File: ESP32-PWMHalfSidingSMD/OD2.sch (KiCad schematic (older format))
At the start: 5 parts, among them IC2 MCT6H, T6 In Track1 Out

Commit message: Update part numbers for ESP32-PWMHalfSidingSMD and created prelim BOM files.
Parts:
- R5: Mouser Part Number 603-CFR-25JR-5210R -> 71-CRCW060310R0FKEAC
- R6: Mouser Part Number 603-CFR25SJT-52-10K -> 71-CRCW060310K0JNEBC
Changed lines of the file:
@@
 F 2 "~" V 2430 1500 30  0000 C CNN
 F 3 "~" H 2500 1500 30  0000 C CNN
-F 4 "603-CFR-25JR-5210R" H 2500 1500 60  0001 C CNN "Mouser Part Number"
+F 4 "71-CRCW060310R0FKEAC" H 2500 1500 60  0001 C CNN "Mouser Part Number"
 	1    2500 1500
 	0    -1   -1   0
@@
 F 2 "~" V 4230 1100 30  0000 C CNN
 F 3 "~" H 4300 1100 30  0000 C CNN
-F 4 "603-CFR25SJT-52-10K" H 4300 1100 60  0001 C CNN "Mouser Part Number"
+F 4 "71-CRCW060310K0JNEBC" H 4300 1100 60  0001 C CNN "Mouser Part Number"
 	1    4300 1100
 	1    0    0    -1

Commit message: Updated ESP32-PWMHalfSidingSMD board.
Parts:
- added D7: LED, LEDs:LED_0603, symbol LED
- added Q2: MMBT3904, TO_SOT_Packages_SMD:SOT-23, symbol MMBT3904
- D5: footprint ~ -> Z4DGP:Z4DGP
- IC2: footprint DIP-8__300 -> SMT8:SMT8
- R5: footprint ~ -> (none); symbol R -> R-RESCUE-ESP32-PWMHalfSidingSMD
- R6: value 10K Ohms -> 2.7K Ohms; footprint ~ -> (none); symbol R -> R-RESCUE-ESP32-PWMHalfSidingSMD
- T6: value In Track1 Out -> In Track2 Out; footprint ~ -> Connectors:bornier2
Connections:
- wire segments 22 -> 26
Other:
- moved on the sheet: R6
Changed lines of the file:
@@
 EESchema Schematic File Version 2
+LIBS:ESP32-PWMHalfSidingSMD-rescue
 LIBS:power
 LIBS:device
@@
 LIBS:memory
 LIBS:xilinx
-LIBS:special
 LIBS:microcontrollers
 LIBS:dsp
@@
 LIBS:4814p-2
 LIBS:ESP32-PWMHalfSidingSMD-cache
-EELAYER 27 0
+EELAYER 25 0
 EELAYER END
 $Descr A4 11693 8268
@@
 AR Path="/5CA368DE/5C8316FA" Ref="T6"  Part="1"
 F 0 "T6" V 1300 1300 40  0000 C CNN
-F 1 "In Track1 Out" V 1400 1300 40  0000 C CNN
-F 2 "~" H 1350 1300 60  0000 C CNN
+F 1 "In Track2 Out" V 1400 1300 40  0000 C CNN
+F 2 "Connectors:bornier2" H 1350 1300 60  0001 C CNN
 F 3 "~" H 1350 1300 60  0000 C CNN
 F 4 " 490-TB007-508-02BE" H 1350 1300 60  0001 C CNN "Mouser Part Number"
@@
 $EndComp
 $Comp
-L R R?
+L R-RESCUE-ESP32-PWMHalfSidingSMD R?
 U 1 1 5CA369C5
 P 2500 1500
@@
 F 0 "R5" V 2580 1500 40  0000 C CNN
 F 1 "10 Ohms" V 2507 1501 40  0000 C CNN
-F 2 "~" V 2430 1500 30  0000 C CNN
+F 2 "" V 2430 1500 30  0001 C CNN
 F 3 "~" H 2500 1500 30  0000 C CNN
 F 4 "71-CRCW060310R0FKEAC" H 2500 1500 60  0001 C CNN "Mouser Part Number"
@@
 F 0 "IC2" H 3490 1790 40  0000 C CNN
 F 1 "MCT6H" H 3810 1410 40  0000 C CNN
-F 2 "DIP-8__300" H 3540 1420 30  0001 C CIN
+F 2 "SMT8:SMT8" H 3540 1420 30  0001 C CIN
 F 3 "~" H 3700 1600 60  0000 C CNN
 F 4 " MCT6SD" H 3700 1600 60  0001 C CNN "Mouser Part Number"
@@
 F 0 "IC2" H 3490 2340 40  0000 C CNN
 F 1 "MCT6H" H 3810 1960 40  0000 C CNN
-F 2 "DIP-8__300" H 3540 1970 30  0001 C CIN
+F 2 "SMT8:SMT8" H 3540 1970 30  0001 C CIN
 F 3 "~" H 3700 2150 60  0000 C CNN
 F 4 " MCT6SD" H 3700 2150 60  0001 C CNN "Mouser Part Number"
@@
 $EndComp
 $Comp
-L R R?
+L R-RESCUE-ESP32-PWMHalfSidingSMD R?
 U 1 1 5CA369C8
-P 4300 1100
+P 5150 1250
 AR Path="/5C70A8FB/5CA369C8" Ref="R?"  Part="1"
 AR Path="/5CA368DE/5CA369C8" Ref="R6"  Part="1"
-F 0 "R6" V 4380 1100 40  0000 C CNN
-F 1 "10K Ohms" V 4307 1101 40  0000 C CNN
-F 2 "~" V 4230 1100 30  0000 C CNN
-F 3 "~" H 4300 1100 30  0000 C CNN
-F 4 "71-CRCW060310K0JNEBC" H 4300 1100 60  0001 C CNN "Mouser Part Number"
-	1    4300 1100
+F 0 "R6" V 5230 1250 40  0000 C CNN
+F 1 "2.7K Ohms" V 5157 1251 40  0000 C CNN
+F 2 "" V 5080 1250 30  0001 C CNN
+F 3 "~" H 5150 1250 30  0000 C CNN
+F 4 "71-CRCW060310K0JNEBC" H 5150 1250 60  0001 C CNN "Mouser Part Number"
+	1    5150 1250
 	1    0    0    -1
 $EndComp
@@
 F 0 "D5" H 2050 3000 70  0000 C CNN
 F 1 "BRIDGEX" H 2050 2900 70  0000 C CNN
-F 2 "~" H 2050 2950 60  0000 C CNN
+F 2 "Z4DGP:Z4DGP" H 2050 2950 60  0001 C CNN
 F 3 "~" H 2050 2950 60  0000 C CNN
 F 4 "Z4DGP406L-HF" H 2050 2950 60  0001 C CNN "Mouser Part Number"
@@
 	4300 2050 4050 2050
 Wire Wire Line
-	4300 1350 4300 2050
-Wire Wire Line
-	4050 1500 4450 1500
+	4300 750  4300 2050
+Wire Wire Line
+	4050 1500 4300 1500
 Wire Wire Line
 	4050 1700 4200 1700
 Wire Wire Line
-	4200 1700 4200 2450
-Wire Wire Line
-	4200 2250 4050 2250
+	4200 1700 4200 2250
+Wire Wire Line
+	4050 2250 4850 2250
 Connection ~ 3200 1500
 Wire Wire Line
@@
 	1    0    0    -1
 $EndComp
-Wire Wire Line
-	4300 750  4300 850
-$Comp
-L GND #PWR?
+$Comp
+L GND-RESCUE-ESP32-PWMHalfSidingSMD #PWR?
 U 1 1 5CA369CA
-P 4200 2450
+P 5150 2700
 AR Path="/5C70AEE5/5CA369CA" Ref="#PWR?"  Part="1"
 AR Path="/5CA368DE/5CA369CA" Ref="#PWR020"  Part="1"
-F 0 "#PWR020" H 4200 2450 30  0001 C CNN
-F 1 "GND" H 4200 2380 30  0001 C CNN
-F 2 "" H 4200 2450 60  0000 C CNN
-F 3 "" H 4200 2450 60  0000 C CNN
-	1    4200 2450
+F 0 "#PWR020" H 5150 2700 30  0001 C CNN
+F 1 "GND" H 5150 2630 30  0001 C CNN
+F 2 "" H 5150 2700 60  0000 C CNN
+F 3 "" H 5150 2700 60  0000 C CNN
+	1    5150 2700
 	1    0    0    -1
 $EndComp
 Connection ~ 4200 2250
-Text HLabel 4450 1500 2    60   Input ~ 0
+Text HLabel 5650 2000 2    60   Input ~ 0
 OD2
 Wire Wire Line
@@
 Wire Wire Line
 	1200 2550 1200 2950
+$Comp
+L MMBT3904 Q2
+U 1 1 60802FE1
+P 5050 2250
+F 0 "Q2" H 5250 2325 50  0000 L CNN
+F 1 "MMBT3904" H 5250 2250 50  0000 L CNN
+F 2 "TO_SOT_Packages_SMD:SOT-23" H 5250 2175 50  0001 L CIN
+F 3 "" H 5050 2250 50  0001 L CNN
+	1    5050 2250
+	1    0    0    -1
+$EndComp
+$Comp
+L LED D7
+U 1 1 60803091
+P 5150 1750
+F 0 "D7" H 5150 1850 50  0000 C CNN
+F 1 "LED" H 5150 1650 50  0000 C CNN
+F 2 "LEDs:LED_0603" H 5150 1750 50  0001 C CNN
+F 3 "" H 5150 1750 50  0001 C CNN
+	1    5150 1750
+	0    -1   -1   0
+$EndComp
+Wire Wire Line
+	5150 1000 4300 1000
+Connection ~ 4300 1000
+Wire Wire Line
+	5150 1500 5150 1600
+Wire Wire Line
+	5150 1900 5150 2050
+Wire Wire Line
+	5150 2450 5150 2700
+Wire Wire Line
+	5650 2000 5150 2000
+Connection ~ 5150 2000
 $EndSCHEMATC

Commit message: Restore PocketBeagleCommandStation_SMD.kicad_pcb
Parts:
- removed D7: LED, LEDs:LED_0603, symbol LED
- removed Q2: MMBT3904, TO_SOT_Packages_SMD:SOT-23, symbol MMBT3904
- D5: footprint Z4DGP:Z4DGP -> ~
- IC2: footprint SMT8:SMT8 -> DIP-8__300
- R5: footprint (none) -> ~; symbol R-RESCUE-ESP32-PWMHalfSidingSMD -> R
- R6: value 2.7K Ohms -> 10K Ohms; footprint (none) -> ~; symbol R-RESCUE-ESP32-PWMHalfSidingSMD -> R
- T6: value In Track2 Out -> In Track1 Out; footprint Connectors:bornier2 -> ~
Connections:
- wire segments 26 -> 22
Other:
- moved on the sheet: R6
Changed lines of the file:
@@
 EESchema Schematic File Version 2
-LIBS:ESP32-PWMHalfSidingSMD-rescue
 LIBS:power
 LIBS:device
@@
 LIBS:memory
 LIBS:xilinx
+LIBS:special
 LIBS:microcontrollers
 LIBS:dsp
@@
 LIBS:4814p-2
 LIBS:ESP32-PWMHalfSidingSMD-cache
-EELAYER 25 0
+EELAYER 27 0
 EELAYER END
 $Descr A4 11693 8268
@@
 AR Path="/5CA368DE/5C8316FA" Ref="T6"  Part="1"
 F 0 "T6" V 1300 1300 40  0000 C CNN
-F 1 "In Track2 Out" V 1400 1300 40  0000 C CNN
-F 2 "Connectors:bornier2" H 1350 1300 60  0001 C CNN
+F 1 "In Track1 Out" V 1400 1300 40  0000 C CNN
+F 2 "~" H 1350 1300 60  0000 C CNN
 F 3 "~" H 1350 1300 60  0000 C CNN
 F 4 " 490-TB007-508-02BE" H 1350 1300 60  0001 C CNN "Mouser Part Number"
@@
 $EndComp
 $Comp
-L R-RESCUE-ESP32-PWMHalfSidingSMD R?
+L R R?
 U 1 1 5CA369C5
 P 2500 1500
@@
 F 0 "R5" V 2580 1500 40  0000 C CNN
 F 1 "10 Ohms" V 2507 1501 40  0000 C CNN
-F 2 "" V 2430 1500 30  0001 C CNN
+F 2 "~" V 2430 1500 30  0000 C CNN
 F 3 "~" H 2500 1500 30  0000 C CNN
 F 4 "71-CRCW060310R0FKEAC" H 2500 1500 60  0001 C CNN "Mouser Part Number"
@@
 F 0 "IC2" H 3490 1790 40  0000 C CNN
 F 1 "MCT6H" H 3810 1410 40  0000 C CNN
-F 2 "SMT8:SMT8" H 3540 1420 30  0001 C CIN
+F 2 "DIP-8__300" H 3540 1420 30  0001 C CIN
 F 3 "~" H 3700 1600 60  0000 C CNN
 F 4 " MCT6SD" H 3700 1600 60  0001 C CNN "Mouser Part Number"
@@
 F 0 "IC2" H 3490 2340 40  0000 C CNN
 F 1 "MCT6H" H 3810 1960 40  0000 C CNN
-F 2 "SMT8:SMT8" H 3540 1970 30  0001 C CIN
+F 2 "DIP-8__300" H 3540 1970 30  0001 C CIN
 F 3 "~" H 3700 2150 60  0000 C CNN
 F 4 " MCT6SD" H 3700 2150 60  0001 C CNN "Mouser Part Number"
@@
 $EndComp
 $Comp
-L R-RESCUE-ESP32-PWMHalfSidingSMD R?
+L R R?
 U 1 1 5CA369C8
-P 5150 1250
+P 4300 1100
 AR Path="/5C70A8FB/5CA369C8" Ref="R?"  Part="1"
 AR Path="/5CA368DE/5CA369C8" Ref="R6"  Part="1"
-F 0 "R6" V 5230 1250 40  0000 C CNN
-F 1 "2.7K Ohms" V 5157 1251 40  0000 C CNN
-F 2 "" V 5080 1250 30  0001 C CNN
-F 3 "~" H 5150 1250 30  0000 C CNN
-F 4 "71-CRCW060310K0JNEBC" H 5150 1250 60  0001 C CNN "Mouser Part Number"
-	1    5150 1250
+F 0 "R6" V 4380 1100 40  0000 C CNN
+F 1 "10K Ohms" V 4307 1101 40  0000 C CNN
+F 2 "~" V 4230 1100 30  0000 C CNN
+F 3 "~" H 4300 1100 30  0000 C CNN
+F 4 "71-CRCW060310K0JNEBC" H 4300 1100 60  0001 C CNN "Mouser Part Number"
+	1    4300 1100
 	1    0    0    -1
 $EndComp
@@
 F 0 "D5" H 2050 3000 70  0000 C CNN
 F 1 "BRIDGEX" H 2050 2900 70  0000 C CNN
-F 2 "Z4DGP:Z4DGP" H 2050 2950 60  0001 C CNN
+F 2 "~" H 2050 2950 60  0000 C CNN
 F 3 "~" H 2050 2950 60  0000 C CNN
 F 4 "Z4DGP406L-HF" H 2050 2950 60  0001 C CNN "Mouser Part Number"
@@
 	4300 2050 4050 2050
 Wire Wire Line
-	4300 750  4300 2050
-Wire Wire Line
-	4050 1500 4300 1500
+	4300 1350 4300 2050
+Wire Wire Line
+	4050 1500 4450 1500
 Wire Wire Line
 	4050 1700 4200 1700
 Wire Wire Line
-	4200 1700 4200 2250
-Wire Wire Line
-	4050 2250 4850 2250
+	4200 1700 4200 2450
+Wire Wire Line
+	4200 2250 4050 2250
 Connection ~ 3200 1500
 Wire Wire Line
@@
 	1    0    0    -1
 $EndComp
-$Comp
-L GND-RESCUE-ESP32-PWMHalfSidingSMD #PWR?
+Wire Wire Line
+	4300 750  4300 850
+$Comp
+L GND #PWR?
 U 1 1 5CA369CA
-P 5150 2700
+P 4200 2450
 AR Path="/5C70AEE5/5CA369CA" Ref="#PWR?"  Part="1"
 AR Path="/5CA368DE/5CA369CA" Ref="#PWR020"  Part="1"
-F 0 "#PWR020" H 5150 2700 30  0001 C CNN
-F 1 "GND" H 5150 2630 30  0001 C CNN
-F 2 "" H 5150 2700 60  0000 C CNN
-F 3 "" H 5150 2700 60  0000 C CNN
-	1    5150 2700
+F 0 "#PWR020" H 4200 2450 30  0001 C CNN
+F 1 "GND" H 4200 2380 30  0001 C CNN
+F 2 "" H 4200 2450 60  0000 C CNN
+F 3 "" H 4200 2450 60  0000 C CNN
+	1    4200 2450
 	1    0    0    -1
 $EndComp
 Connection ~ 4200 2250
-Text HLabel 5650 2000 2    60   Input ~ 0
+Text HLabel 4450 1500 2    60   Input ~ 0
 OD2
 Wire Wire Line
@@
 Wire Wire Line
 	1200 2550 1200 2950
-$Comp
-L MMBT3904 Q2
-U 1 1 60802FE1
-P 5050 2250
-F 0 "Q2" H 5250 2325 50  0000 L CNN
-F 1 "MMBT3904" H 5250 2250 50  0000 L CNN
-F 2 "TO_SOT_Packages_SMD:SOT-23" H 5250 2175 50  0001 L CIN
-F 3 "" H 5050 2250 50  0001 L CNN
-	1    5050 2250
-	1    0    0    -1
-$EndComp
-$Comp
-L LED D7
-U 1 1 60803091
-P 5150 1750
-F 0 "D7" H 5150 1850 50  0000 C CNN
-F 1 "LED" H 5150 1650 50  0000 C CNN
-F 2 "LEDs:LED_0603" H 5150 1750 50  0001 C CNN
-F 3 "" H 5150 1750 50  0001 C CNN
-	1    5150 1750
-	0    -1   -1   0
-$EndComp
-Wire Wire Line
-	5150 1000 4300 1000
-Connection ~ 4300 1000
-Wire Wire Line
-	5150 1500 5150 1600
-Wire Wire Line
-	5150 1900 5150 2050
-Wire Wire Line
-	5150 2450 5150 2700
-Wire Wire Line
-	5650 2000 5150 2000
-Connection ~ 5150 2000
 $EndSCHEMATC

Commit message: Repair ESP32-PWMHalfSidingSMD and generate POS file.
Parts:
- added D7: LED, LEDs:LED_0603, symbol LED
- added Q2: MMBT3904, TO_SOT_Packages_SMD:SOT-23, symbol MMBT3904
- D5: footprint ~ -> Z4DGP:Z4DGP
- IC2: footprint DIP-8__300 -> SMT8:SMT8
- R5: footprint ~ -> Resistors_SMD:R_0603; symbol R -> R-RESCUE-ESP32-PWMHalfSidingSMD
- R6: value 10K Ohms -> 2.7K Ohms; footprint ~ -> Resistors_SMD:R_0603; symbol R -> R-RESCUE-ESP32-PWMHalfSidingSMD
- T6: footprint ~ -> Connectors:bornier2
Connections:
- wire segments 22 -> 26
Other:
- moved on the sheet: R6
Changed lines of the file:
@@
 EESchema Schematic File Version 2
+LIBS:ESP32-PWMHalfSidingSMD-rescue
 LIBS:power
 LIBS:device
@@
 LIBS:memory
 LIBS:xilinx
-LIBS:special
 LIBS:microcontrollers
 LIBS:dsp
@@
 LIBS:4814p-2
 LIBS:ESP32-PWMHalfSidingSMD-cache
-EELAYER 27 0
+EELAYER 25 0
 EELAYER END
 $Descr A4 11693 8268
@@
 F 0 "T6" V 1300 1300 40  0000 C CNN
 F 1 "In Track1 Out" V 1400 1300 40  0000 C CNN
-F 2 "~" H 1350 1300 60  0000 C CNN
+F 2 "Connectors:bornier2" H 1350 1300 60  0001 C CNN
 F 3 "~" H 1350 1300 60  0000 C CNN
 F 4 " 490-TB007-508-02BE" H 1350 1300 60  0001 C CNN "Mouser Part Number"
@@
 $EndComp
 $Comp
-L R R?
+L R-RESCUE-ESP32-PWMHalfSidingSMD R?
 U 1 1 5CA369C5
 P 2500 1500
@@
 F 0 "R5" V 2580 1500 40  0000 C CNN
 F 1 "10 Ohms" V 2507 1501 40  0000 C CNN
-F 2 "~" V 2430 1500 30  0000 C CNN
+F 2 "Resistors_SMD:R_0603" V 2430 1500 30  0001 C CNN
 F 3 "~" H 2500 1500 30  0000 C CNN
 F 4 "71-CRCW060310R0FKEAC" H 2500 1500 60  0001 C CNN "Mouser Part Number"
@@
 F 0 "IC2" H 3490 1790 40  0000 C CNN
 F 1 "MCT6H" H 3810 1410 40  0000 C CNN
-F 2 "DIP-8__300" H 3540 1420 30  0001 C CIN
+F 2 "SMT8:SMT8" H 3540 1420 30  0001 C CIN
 F 3 "~" H 3700 1600 60  0000 C CNN
 F 4 " MCT6SD" H 3700 1600 60  0001 C CNN "Mouser Part Number"
@@
 F 0 "IC2" H 3490 2340 40  0000 C CNN
 F 1 "MCT6H" H 3810 1960 40  0000 C CNN
-F 2 "DIP-8__300" H 3540 1970 30  0001 C CIN
+F 2 "SMT8:SMT8" H 3540 1970 30  0001 C CIN
 F 3 "~" H 3700 2150 60  0000 C CNN
 F 4 " MCT6SD" H 3700 2150 60  0001 C CNN "Mouser Part Number"
@@
 $EndComp
 $Comp
-L R R?
+L R-RESCUE-ESP32-PWMHalfSidingSMD R?
 U 1 1 5CA369C8
-P 4300 1100
+P 4700 1300
 AR Path="/5C70A8FB/5CA369C8" Ref="R?"  Part="1"
 AR Path="/5CA368DE/5CA369C8" Ref="R6"  Part="1"
-F 0 "R6" V 4380 1100 40  0000 C CNN
-F 1 "10K Ohms" V 4307 1101 40  0000 C CNN
-F 2 "~" V 4230 1100 30  0000 C CNN
-F 3 "~" H 4300 1100 30  0000 C CNN
-F 4 "71-CRCW060310K0JNEBC" H 4300 1100 60  0001 C CNN "Mouser Part Number"
-	1    4300 1100
+F 0 "R6" V 4780 1300 40  0000 C CNN
+F 1 "2.7K Ohms" V 4707 1301 40  0000 C CNN
+F 2 "Resistors_SMD:R_0603" V 4630 1300 30  0001 C CNN
+F 3 "~" H 4700 1300 30  0000 C CNN
+F 4 "71-CRCW060310K0JNEBC" H 4700 1300 60  0001 C CNN "Mouser Part Number"
+	1    4700 1300
 	1    0    0    -1
 $EndComp
@@
 Wire Wire Line
 	1250 1900 1250 1650
-$Comp
-L BRIDGEX D?
-U 1 1 5CA369C4
-P 2050 2950
-AR Path="/5C70A8FB/5CA369C4" Ref="D?"  Part="1"
-AR Path="/5CA368DE/5CA369C4" Ref="D5"  Part="1"
-F 0 "D5" H 2050 3000 70  0000 C CNN
-F 1 "BRIDGEX" H 2050 2900 70  0000 C CNN
-F 2 "~" H 2050 2950 60  0000 C CNN
-F 3 "~" H 2050 2950 60  0000 C CNN
-F 4 "Z4DGP406L-HF" H 2050 2950 60  0001 C CNN "Mouser Part Number"
-	1    2050 2950
-	0    1    1    0
-$EndComp
 Wire Wire Line
 	2050 2100 2050 3800
@@
 	4300 2050 4050 2050
 Wire Wire Line
-	4300 1350 4300 2050
-Wire Wire Line
-	4050 1500 4450 1500
+	4300 750  4300 2050
 Wire Wire Line
 	4050 1700 4200 1700
 Wire Wire Line
-	4200 1700 4200 2450
-Wire Wire Line
-	4200 2250 4050 2250
+	4050 2250 4400 2250
 Connection ~ 3200 1500
 Wire Wire Line
@@
 	1    0    0    -1
 $EndComp
-Wire Wire Line
-	4300 750  4300 850
-$Comp
-L GND #PWR?
+$Comp
+L GND-RESCUE-ESP32-PWMHalfSidingSMD #PWR?
 U 1 1 5CA369CA
-P 4200 2450
+P 4700 2650
 AR Path="/5C70AEE5/5CA369CA" Ref="#PWR?"  Part="1"
 AR Path="/5CA368DE/5CA369CA" Ref="#PWR020"  Part="1"
-F 0 "#PWR020" H 4200 2450 30  0001 C CNN
-F 1 "GND" H 4200 2380 30  0001 C CNN
-F 2 "" H 4200 2450 60  0000 C CNN
-F 3 "" H 4200 2450 60  0000 C CNN
-	1    4200 2450
+F 0 "#PWR020" H 4700 2650 30  0001 C CNN
+F 1 "GND" H 4700 2580 30  0001 C CNN
+F 2 "" H 4700 2650 60  0000 C CNN
+F 3 "" H 4700 2650 60  0000 C CNN
+	1    4700 2650
 	1    0    0    -1
 $EndComp
 Connection ~ 4200 2250
-Text HLabel 4450 1500 2    60   Input ~ 0
+Text HLabel 5050 2000 2    60   Input ~ 0
 OD2
 Wire Wire Line
@@
 Wire Wire Line
 	1200 2550 1200 2950
+$Comp
+L MMBT3904 Q2
+U 1 1 608C00C3
+P 4600 2250
+F 0 "Q2" H 4800 2325 50  0000 L CNN
+F 1 "MMBT3904" H 4800 2250 50  0000 L CNN
+F 2 "TO_SOT_Packages_SMD:SOT-23" H 4800 2175 50  0001 L CIN
+F 3 "" H 4600 2250 50  0001 L CNN
+	1    4600 2250
+	1    0    0    -1
+$EndComp
+$Comp
+L LED D7
+U 1 1 608C015E
+P 4700 1800
+F 0 "D7" H 4700 1900 50  0000 C CNN
+F 1 "LED" H 4700 1700 50  0000 C CNN
+F 2 "LEDs:LED_0603" H 4700 1800 50  0001 C CNN
+F 3 "" H 4700 1800 50  0001 C CNN
+	1    4700 1800
+	0    -1   -1   0
+$EndComp
+Wire Wire Line
+	4200 1700 4200 2250
+Wire Wire Line
+	4050 1500 4300 1500
+Wire Wire Line
+	4700 2450 4700 2650
+Wire Wire Line
+	4700 1050 4300 1050
+Connection ~ 4300 1050
+Wire Wire Line
+	4700 1550 4700 1650
+Wire Wire Line
+	4700 1950 4700 2050
+Wire Wire Line
+	5050 2000 4700 2000
+Connection ~ 4700 2000
+$Comp
+L BRIDGEX D?
+U 1 1 5CA369C4
+P 2050 2950
+AR Path="/5C70A8FB/5CA369C4" Ref="D?"  Part="1"
+AR Path="/5CA368DE/5CA369C4" Ref="D5"  Part="1"
+F 0 "D5" H 2050 3000 70  0000 C CNN
+F 1 "BRIDGEX" H 2050 2900 70  0000 C CNN
+F 2 "Z4DGP:Z4DGP" H 2050 2950 60  0001 C CNN
+F 3 "~" H 2050 2950 60  0000 C CNN
+F 4 "Z4DGP406L-HF" H 2050 2950 60  0001 C CNN "Mouser Part Number"
+	1    2050 2950
+	0    1    1    0
+$EndComp
 $EndSCHEMATC

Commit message: Generate BOM for ESP32-PWMHalfSidingSMD.
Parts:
- D5: Mouser Part Number Z4DGP406L-HF -> 750-Z4DGP406L-HF
- D7: Mouser Part Number (none) -> 710-150060SS55040
- IC2: Mouser Part Number MCT6SD -> 512-MCT6SD
- Q2: Mouser Part Number (none) -> 771-MMBT3904T/R
- R6: Mouser Part Number 71-CRCW060310K0JNEBC -> 71-CRCW06032K70JNEAC
- T6: Mouser Part Number 490-TB007-508-02BE -> 490-TB007-508-02BE
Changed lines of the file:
@@
 F 2 "Connectors:bornier2" H 1350 1300 60  0001 C CNN
 F 3 "~" H 1350 1300 60  0000 C CNN
-F 4 " 490-TB007-508-02BE" H 1350 1300 60  0001 C CNN "Mouser Part Number"
+F 4 "490-TB007-508-02BE" H 1350 1300 60  0001 C CNN "Mouser Part Number"
 	1    1350 1300
 	0    -1   -1   0
@@
 F 2 "SMT8:SMT8" H 3540 1420 30  0001 C CIN
 F 3 "~" H 3700 1600 60  0000 C CNN
-F 4 " MCT6SD" H 3700 1600 60  0001 C CNN "Mouser Part Number"
+F 4 "512-MCT6SD" H 3700 1600 60  0001 C CNN "Mouser Part Number"
 	1    3700 1600
 	1    0    0    -1
@@
 F 2 "Resistors_SMD:R_0603" V 4630 1300 30  0001 C CNN
 F 3 "~" H 4700 1300 30  0000 C CNN
-F 4 "71-CRCW060310K0JNEBC" H 4700 1300 60  0001 C CNN "Mouser Part Number"
+F 4 "71-CRCW06032K70JNEAC" H 4700 1300 60  0001 C CNN "Mouser Part Number"
 	1    4700 1300
 	1    0    0    -1
@@
 F 2 "TO_SOT_Packages_SMD:SOT-23" H 4800 2175 50  0001 L CIN
 F 3 "" H 4600 2250 50  0001 L CNN
+F 4 "771-MMBT3904T/R" H 4600 2250 60  0001 C CNN "Mouser Part Number"
 	1    4600 2250
 	1    0    0    -1
@@
 F 2 "LEDs:LED_0603" H 4700 1800 50  0001 C CNN
 F 3 "" H 4700 1800 50  0001 C CNN
+F 4 "710-150060SS55040" H 4700 1800 60  0001 C CNN "Mouser Part Number"
 	1    4700 1800
 	0    -1   -1   0
@@
 F 2 "Z4DGP:Z4DGP" H 2050 2950 60  0001 C CNN
 F 3 "~" H 2050 2950 60  0000 C CNN
-F 4 "Z4DGP406L-HF" H 2050 2950 60  0001 C CNN "Mouser Part Number"
+F 4 "750-Z4DGP406L-HF" H 2050 2950 60  0001 C CNN "Mouser Part Number"
 	1    2050 2950
 	0    1    1    0

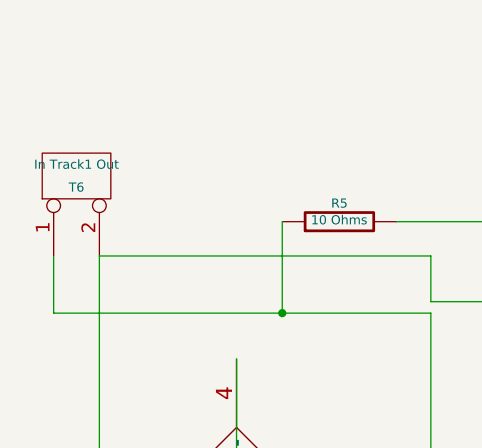
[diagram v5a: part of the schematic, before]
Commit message: Complete 3D view of ESP32-PWMHalfSidingSMD.
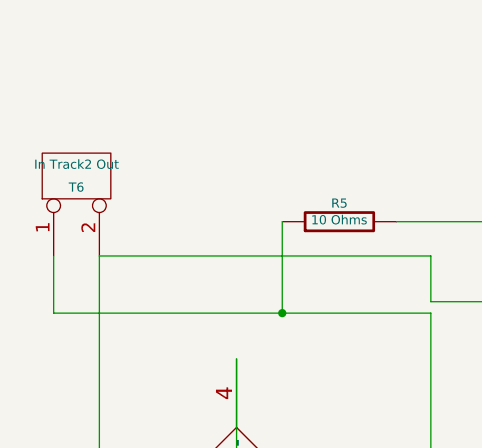
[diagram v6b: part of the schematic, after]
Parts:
- T6: value In Track1 Out -> In Track2 Out
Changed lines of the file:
@@
 EESchema Schematic File Version 2
-LIBS:ESP32-PWMHalfSidingSMD-rescue
 LIBS:power
 LIBS:device
@@
 AR Path="/5CA368DE/5C8316FA" Ref="T6"  Part="1"
 F 0 "T6" V 1300 1300 40  0000 C CNN
-F 1 "In Track1 Out" V 1400 1300 40  0000 C CNN
+F 1 "In Track2 Out" V 1400 1300 40  0000 C CNN
 F 2 "Connectors:bornier2" H 1350 1300 60  0001 C CNN
 F 3 "~" H 1350 1300 60  0000 C CNN
